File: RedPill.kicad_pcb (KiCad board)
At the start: 4 copper layers, 20.4 x 50.9 mm, 43 parts, among them J1 Conn_01x20, J2 Conn_01x20, J3 USB_C_Receptacle_USB2.0, J4 TagConnect_TC2030_SWD, J5 Conn_01x04, J6 Micro_SD_Card, SW1 SW_Push, U1 STM32F722RETx, U2 SRV05-4, U3 XC6206PxxxMR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

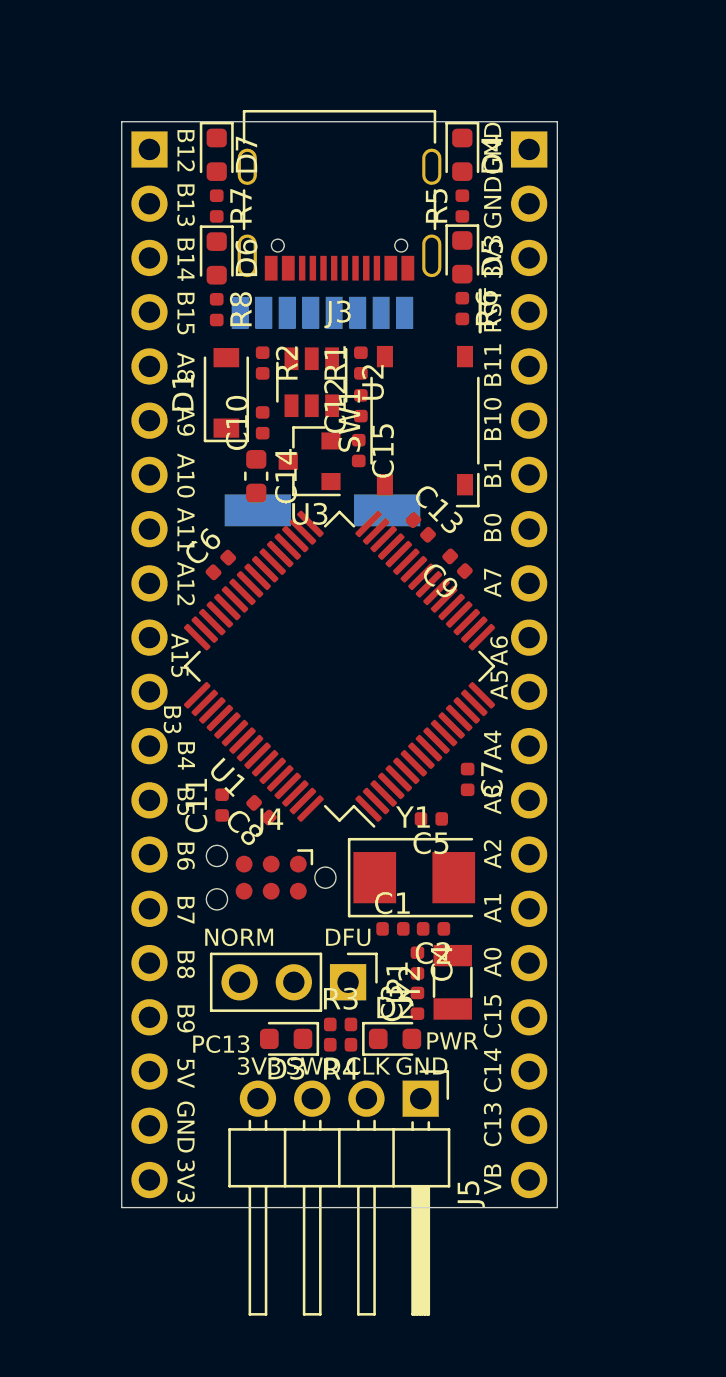
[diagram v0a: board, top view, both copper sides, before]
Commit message: Hide all fp references
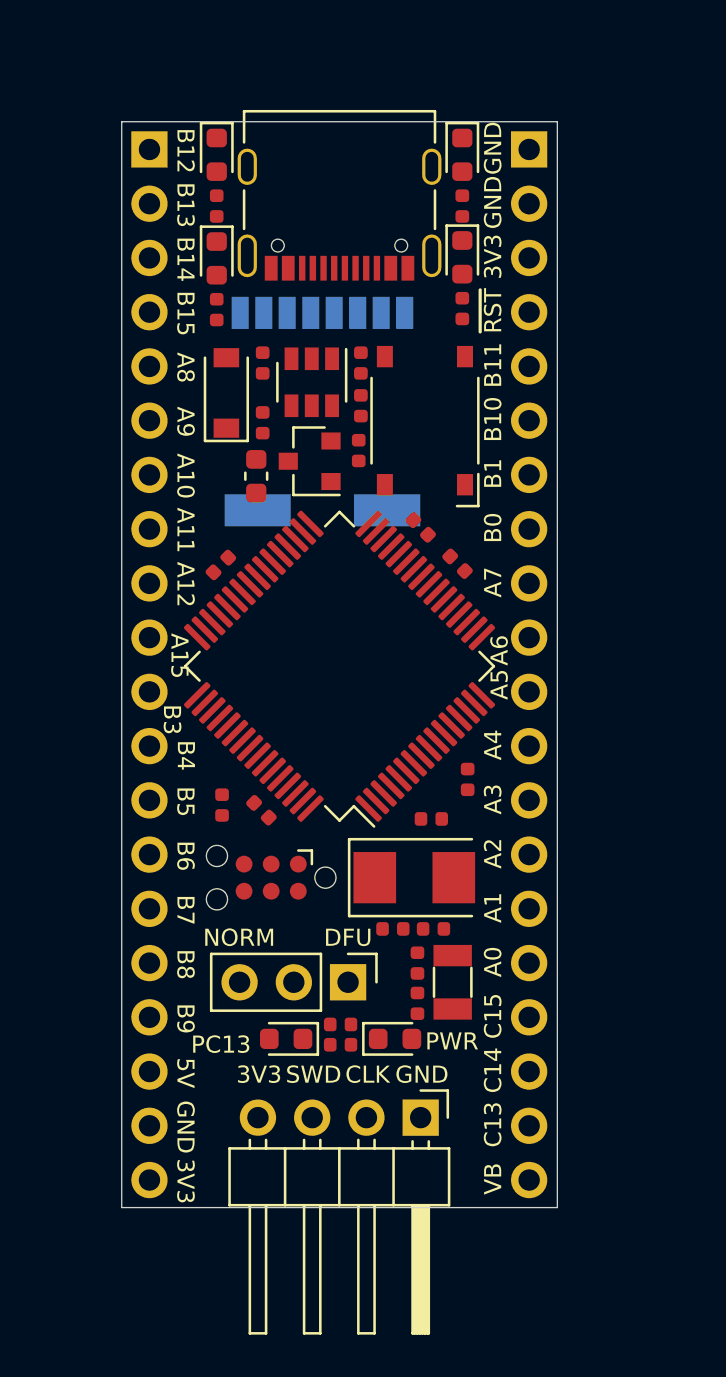
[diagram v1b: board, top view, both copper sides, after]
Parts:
- moved J5 0.89 mm to (112.7, 145.3)

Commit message: Route IOs
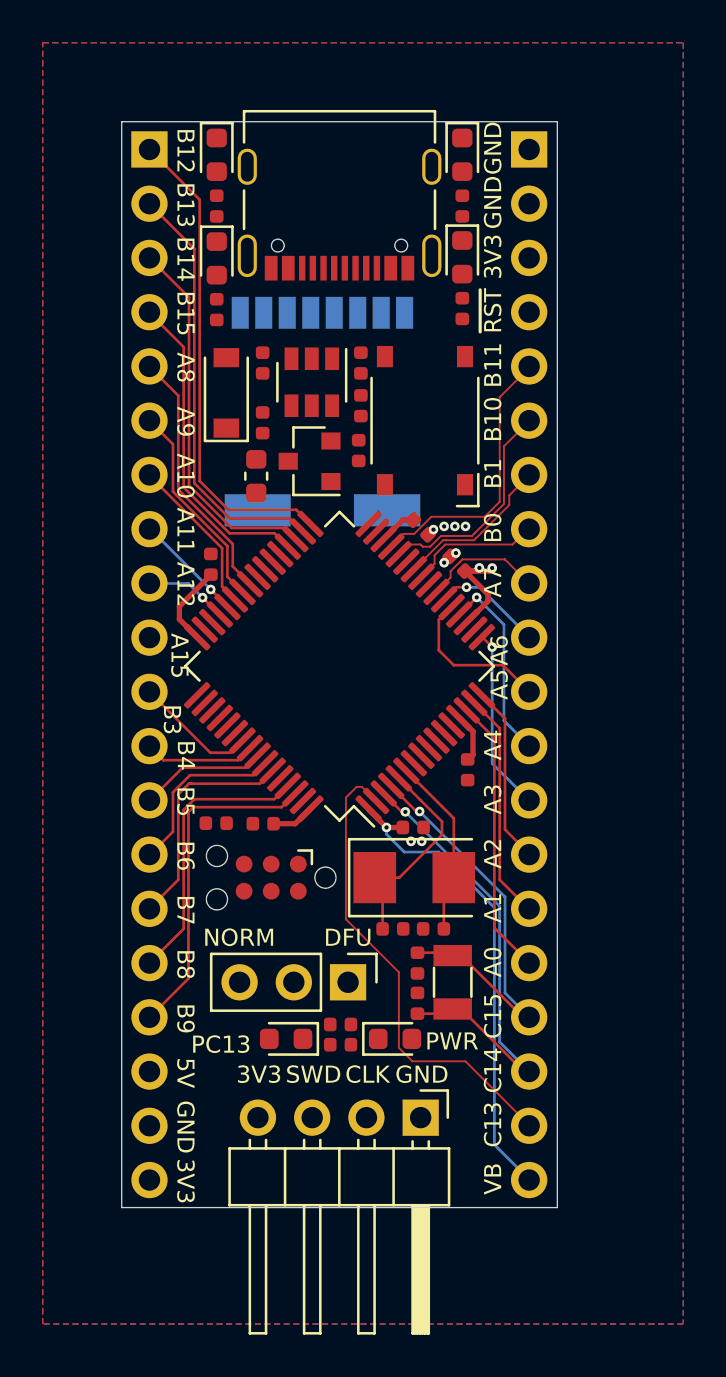
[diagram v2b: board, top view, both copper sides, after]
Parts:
- moved C5 0.94 mm to (112.3, 131.8)
- moved C11 0.89 mm to (103.1, 131.6), turned to 180 degrees
- moved C8 0.64 mm to (105.3, 131.6), turned to 180 degrees
- moved C6 0.47 mm to (102.9, 119.4), turned to 90 degrees
- moved C7 0.45 mm to (114.9, 129.1)
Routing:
- net /PB12: track 0.00 -> 22.5 mm
- net /PC13: track 0.00 -> 22.2 mm
- net /VBAT: track 0.00 -> 22.2 mm, vias 0 -> 1
- net /PC14: track 0.00 -> 22.1 mm, vias 0 -> 1
- net /PB13: track 0.00 -> 20.0 mm
- net /PC15: track 0.00 -> 19.9 mm, vias 0 -> 1
- net /PB14: track 0.00 -> 17.4 mm
- net /PB9: track 0.00 -> 15.8 mm
- net /PB15: track 0.00 -> 14.9 mm
- net +3V3: track 0.00 -> 13.7 mm, vias 0 -> 2
- net /PB8: track 0.00 -> 13.2 mm
- net /PA0: track 0.00 -> 13.1 mm
- net /PB11: track 0.00 -> 12.8 mm
- net /PA8: track 0.00 -> 12.1 mm
- net /PB7: track 0.00 -> 10.9 mm
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- added copper zone on Power, net +3V3
- added copper zone on B.Cu, net GND
- added copper zone on F.Cu, net GND
- added copper zone on GND, net GND

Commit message: Finish layout
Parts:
- added C16: 100nF, Capacitor_SMD:C_0402_1005Metric, F.Cu at (109.8, 116.0)
- moved C12 2.16 mm to (109.8, 114.2), turned to 270 degrees
- moved C15 2.10 mm to (109.9, 112.0), turned to 90 degrees
- turned C11 to 0 degrees
- turned R5 to 270 degrees
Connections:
- U2 pad 1: /D- -> /D+
- U2 pad 3: /D+ -> /D-
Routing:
- net /~RST: track 0.00 -> 42.2 mm, vias 0 -> 4
- net +5V: track 0.00 -> 42.1 mm, vias 0 -> 3
- net Net-(R8-Pad2): track 0.00 -> 40.2 mm, vias 0 -> 2
- net Net-(R7-Pad2): track 0.00 -> 40.2 mm, vias 0 -> 2
- net /SWCLK: track 0.00 -> 30.2 mm, vias 0 -> 2
- net Net-(R5-Pad2): track 0.00 -> 29.6 mm, vias 0 -> 2
- net /SWDIO: track 0.00 -> 26.9 mm, vias 0 -> 2
- net /D+: track 3.90 -> 29.1 mm, vias 1 -> 3
- net Net-(R6-Pad2): track 0.00 -> 24.1 mm, vias 0 -> 2
- net Net-(D1-Pad2): track 0.00 -> 23.9 mm, vias 0 -> 2
- net /D-: track 5.15 -> 28.9 mm, vias 1 -> 5
- net /SD_DAT2: track 0.00 -> 22.3 mm, vias 0 -> 1
- net /SD_DAT3: track 0.00 -> 22.1 mm, vias 0 -> 1
- net /SD_CMD: track 0.00 -> 22.1 mm, vias 0 -> 1
- net /SD_CLK: track 0.00 -> 21.5 mm, vias 0 -> 1
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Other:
- board text added: "RedPill RevA"

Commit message: Add JLCSMT tooling holes
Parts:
- added H1: ToolingHole, ToolingHole:ToolingHole_JLCSMT, F.Cu at (106.0, 100.6)
- added H2: ToolingHole, ToolingHole:ToolingHole_JLCSMT, F.Cu at (113.2, 147.9)
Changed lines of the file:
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@@
     (tracks 627)
     (zones 0)
-    (modules 44)
+    (modules 46)
     (nets 72)
   )
@@
     (add_net GND)
   )
+  (module ToolingHole:ToolingHole_JLCSMT (layer F.Cu)
+    (at 113.2 147.9)
+    (fp_text reference H2 (at 0 0.5) (layer F.SilkS) hide
+      (effects (font (size 1 1) (thickness 0.15)))
+    )
+    (fp_text value ToolingHole (at 0 -0.5) (layer F.Fab)
+      (effects (font (size 1 1) (thickness 0.15)))
+    )
+    (fp_text user "tooling hole" (at 0 2.6) (layer F.SilkS)
+      (effects (font (size 1 1) (thickness 0.15)))
+    )
+    (pad "" np_thru_hole circle (at 0 0) (size 1.152 1.152) (drill 1.152) (layers *.Cu *.Mask))
+  )
+  (module ToolingHole:ToolingHole_JLCSMT (layer F.Cu)
+    (at 106 100.6)
+    (fp_text reference H1 (at 0 0.5) (layer F.SilkS) hide
+      (effects (font (size 1 1) (thickness 0.15)))
+    )
+    (fp_text value ToolingHole (at 0 -0.5) (layer F.Fab)
+      (effects (font (size 1 1) (thickness 0.15)))
+    )
+    (fp_text user "tooling hole" (at 0 -3.6) (layer F.SilkS)
+      (effects (font (size 1 1) (thickness 0.15)))
+    )
+    (pad "" np_thru_hole circle (at 0 0) (size 1.152 1.152) (drill 1.152) (layers *.Cu *.Mask))
+  )
   (module Capacitor_SMD:C_0402_1005Metric (layer F.Cu)
     (at 109.75 116.05 270)
@@
     (tags capacitor)
     (attr smd)
-    (fp_text reference C16 (at 0 -1.17 90) (layer F.SilkS)
+    (fp_text reference C16 (at 0 -1.17 90) (layer F.SilkS) hide
       (effects (font (size 1 1) (thickness 0.15)))
     )
@@
     (connect_pads yes (clearance 0.127))
     (min_thickness 0.127)
-    (fill yes (arc_segments 32) (thermal_gap 0.508) (thermal_bridge_width 0.508))
+    (fill (arc_segments 32) (thermal_gap 0.508) (thermal_bridge_width 0.508))
     (polygon
       (pts
@@
     (connect_pads yes (clearance 0.127))
     (min_thickness 0.127)
-    (fill yes (arc_segments 32) (thermal_gap 0.508) (thermal_bridge_width 0.508))
+    (fill (arc_segments 32) (thermal_gap 0.508) (thermal_bridge_width 0.508))
     (polygon
       (pts
@@
     (connect_pads yes (clearance 0.127))
     (min_thickness 0.127)
-    (fill yes (arc_segments 32) (thermal_gap 0.508) (thermal_bridge_width 0.508))
+    (fill (arc_segments 32) (thermal_gap 0.508) (thermal_bridge_width 0.508))
     (polygon
       (pts
@@
     (connect_pads yes (clearance 0.127))
     (min_thickness 0.127)
-    (fill yes (arc_segments 32) (thermal_gap 0.508) (thermal_bridge_width 0.508))
+    (fill (arc_segments 32) (thermal_gap 0.508) (thermal_bridge_width 0.508))
     (polygon
       (pts

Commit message: Add silkscreen markings
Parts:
- added H3: Icon, Icon:pill, B.Cu at (105.3, 127.4)
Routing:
- net GND: vias 51 -> 62
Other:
- board text added: "Designed by"
- board text added: "JLCJLCJLCJLC"
- board text added: "RST"
- board text added: "Tobias Schramm"
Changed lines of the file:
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@@
   (general
     (thickness 1.6)
-    (drawings 57)
-    (tracks 627)
+    (drawings 62)
+    (tracks 638)
     (zones 0)
-    (modules 46)
+    (modules 47)
     (nets 72)
   )
@@
     (add_net GND)
   )
+  (module Icon:pill (layer B.Cu)
+    (at 105.3 127.4 270)
+    (fp_text reference H3 (at 0 0 90) (layer B.SilkS) hide
+      (effects (font (size 1.524 1.524) (thickness 0.3)) (justify mirror))
+    )
+    (fp_text value Icon (at 0.75 0 90) (layer B.SilkS) hide
+      (effects (font (size 1.524 1.524) (thickness 0.3)) (justify mirror))
+    )
+    (fp_poly (pts (xy 4.335025 2.18718) (xy 4.855331 1.860237) (xy 5.286541 1.408233) (xy 5.60285 0.870339)
+      (xy 5.778453 0.285727) (xy 5.805714 -0.045357) (xy 5.716775 -0.663694) (xy 5.456452 -1.249548)
+      (xy 5.040559 -1.774845) (xy 4.859372 -1.952652) (xy 4.691112 -2.100551) (xy 4.517726 -2.221264)
+      (xy 4.321158 -2.317512) (xy 4.083354 -2.392018) (xy 3.786259 -2.447504) (xy 3.411819 -2.486691)
+      (xy 2.941979 -2.512303) (xy 2.358684 -2.527062) (xy 1.64388 -2.533688) (xy 0.779513 -2.534905)
+      (xy 0.006214 -2.533878) (xy -1.020452 -2.530098) (xy -1.877205 -2.522334) (xy -2.575525 -2.510242)
+      (xy -3.12689 -2.493478) (xy -3.54278 -2.471697) (xy -3.834675 -2.444554) (xy -4.007707 -2.413455)
+      (xy -4.573147 -2.172) (xy -5.0538 -1.792104) (xy -5.429138 -1.304993) (xy -5.678631 -0.741894)
+      (xy -5.781752 -0.134031) (xy -5.776946 -0.036215) (xy -5.170209 -0.036215) (xy -5.085822 -0.537658)
+      (xy -4.856671 -1.010362) (xy -4.51478 -1.410362) (xy -4.092172 -1.693692) (xy -3.912429 -1.763062)
+      (xy -3.706241 -1.801972) (xy -3.377697 -1.835797) (xy -2.960198 -1.863844) (xy -2.487149 -1.885418)
+      (xy -1.991954 -1.899828) (xy -1.508015 -1.906379) (xy -1.068736 -1.904378) (xy -0.70752 -1.893132)
+      (xy -0.457772 -1.871949) (xy -0.352893 -1.840133) (xy -0.351737 -1.836965) (xy -0.34684 -1.729)
+      (xy -0.339806 -1.468761) (xy -0.33128 -1.085377) (xy -0.321906 -0.607982) (xy -0.312329 -0.065706)
+      (xy -0.311612 -0.022679) (xy -0.282606 1.723571) (xy -2.049917 1.723571) (xy -2.671348 1.721929)
+      (xy -3.140305 1.715359) (xy -3.485725 1.701398) (xy -3.736545 1.677582) (xy -3.921702 1.641449)
+      (xy -4.070134 1.590534) (xy -4.171216 1.54298) (xy -4.55282 1.262927) (xy -4.870309 0.870307)
+      (xy -5.087996 0.421534) (xy -5.170193 -0.026978) (xy -5.170209 -0.036215) (xy -5.776946 -0.036215)
+      (xy -5.762589 0.255917) (xy -5.593607 0.851309) (xy -5.273901 1.398602) (xy -4.833837 1.860773)
+      (xy -4.303781 2.200798) (xy -4.09766 2.285864) (xy -3.964417 2.316936) (xy -3.746795 2.342549)
+      (xy -3.430806 2.363102) (xy -3.002465 2.378995) (xy -2.447786 2.390624) (xy -1.752783 2.39839)
+      (xy -0.903469 2.40269) (xy 0.045357 2.403928) (xy 3.855357 2.403928) (xy 4.335025 2.18718)) (layer B.SilkS) (width 0.01))
+  )
   (module ToolingHole:ToolingHole_JLCSMT (layer F.Cu)
     (at 113.2 147.9)
@@
     )
   )
+  (gr_text JLCJLCJLCJLC (at 108.9 124.2) (layer F.SilkS)
+    (effects (font (size 1 1) (thickness 0.15)))
+  )
+  (gr_text "Tobias Schramm" (at 109.8 127.9 270) (layer B.SilkS)
+    (effects (font (size 1.5 1.5) (thickness 0.25)) (justify mirror))
+  )
+  (gr_text "Designed by" (at 112.6 135.6 270) (layer B.SilkS)
+    (effects (font (size 1.5 1.5) (thickness 0.25)) (justify mirror))
+  )
+  (gr_text "RedPill RevA" (at 115.1 141.4 270) (layer B.SilkS)
+    (effects (font (size 1.5 1.5) (thickness 0.25)) (justify mirror))
+  )
+  (gr_text RST (at 112.9 116) (layer F.SilkS)
+    (effects (font (size 0.8 0.8) (thickness 0.15)))
+  )
   (gr_text "RedPill RevA" (at 108.8 107.65) (layer F.SilkS)
     (effects (font (size 1 1) (thickness 0.15)))
@@
   (via (at 105.7 106.45) (size 0.45) (drill 0.2) (layers F.Cu B.Cu) (net 5))
   (via (at 105.85 108.85) (size 0.45) (drill 0.2) (layers F.Cu B.Cu) (net 5))
+  (via (at 109.9 118.6) (size 0.45) (drill 0.2) (layers F.Cu B.Cu) (net 5))
+  (via (at 111.9 115.8) (size 0.45) (drill 0.2) (layers F.Cu B.Cu) (net 5))
+  (via (at 115.8 107.8) (size 0.45) (drill 0.2) (layers F.Cu B.Cu) (net 5))
+  (via (at 113.3 108.3) (size 0.45) (drill 0.2) (layers F.Cu B.Cu) (net 5))
+  (via (at 112.1 106.5) (size 0.45) (drill 0.2) (layers F.Cu B.Cu) (net 5))
+  (via (at 102.7 132.3) (size 0.45) (drill 0.2) (layers F.Cu B.Cu) (net 5))
+  (via (at 105 135.8) (size 0.45) (drill 0.2) (layers F.Cu B.Cu) (net 5))
+  (via (at 100.6 116.6) (size 0.45) (drill 0.2) (layers F.Cu B.Cu) (net 5))
+  (via (at 100.6 119.1) (size 0.45) (drill 0.2) (layers F.Cu B.Cu) (net 5))
+  (via (at 116.8 109.3) (size 0.45) (drill 0.2) (layers F.Cu B.Cu) (net 5))
+  (via (at 117.3 147) (size 0.45) (drill 0.2) (layers F.Cu B.Cu) (net 5))
   (segment (start 110.55 134.1) (end 110.55 133.9) (width 0.127) (layer F.Cu) (net 6))
   (segment (start 110.915 136.5) (end 110.915 134.35) (width 0.127) (layer F.Cu) (net 6))
@@
     (connect_pads yes (clearance 0.127))
     (min_thickness 0.127)
-    (fill (arc_segments 32) (thermal_gap 0.508) (thermal_bridge_width 0.508))
+    (fill yes (arc_segments 32) (thermal_gap 0.508) (thermal_bridge_width 0.508))
     (polygon
       (pts
@@
     (connect_pads yes (clearance 0.127))
     (min_thickness 0.127)
-    (fill (arc_segments 32) (thermal_gap 0.508) (thermal_bridge_width 0.508))
+    (fill yes (arc_segments 32) (thermal_gap 0.508) (thermal_bridge_width 0.508))
     (polygon
       (pts
@@
     (connect_pads yes (clearance 0.127))
     (min_thickness 0.127)
-    (fill (arc_segments 32) (thermal_gap 0.508) (thermal_bridge_width 0.508))
+    (fill yes (arc_segments 32) (thermal_gap 0.508) (thermal_bridge_width 0.508))
     (polygon
       (pts
@@
     (connect_pads yes (clearance 0.127))
     (min_thickness 0.127)
-    (fill (arc_segments 32) (thermal_gap 0.508) (thermal_bridge_width 0.508))
+    (fill yes (arc_segments 32) (thermal_gap 0.508) (thermal_bridge_width 0.508))
     (polygon
       (pts
